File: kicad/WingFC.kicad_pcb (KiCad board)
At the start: 4 copper layers, 32 x 33.2 mm, 50 parts, among them U1 XIAO-nRF52840-Plus-SMD, U2 MP2315, U3 DPS310

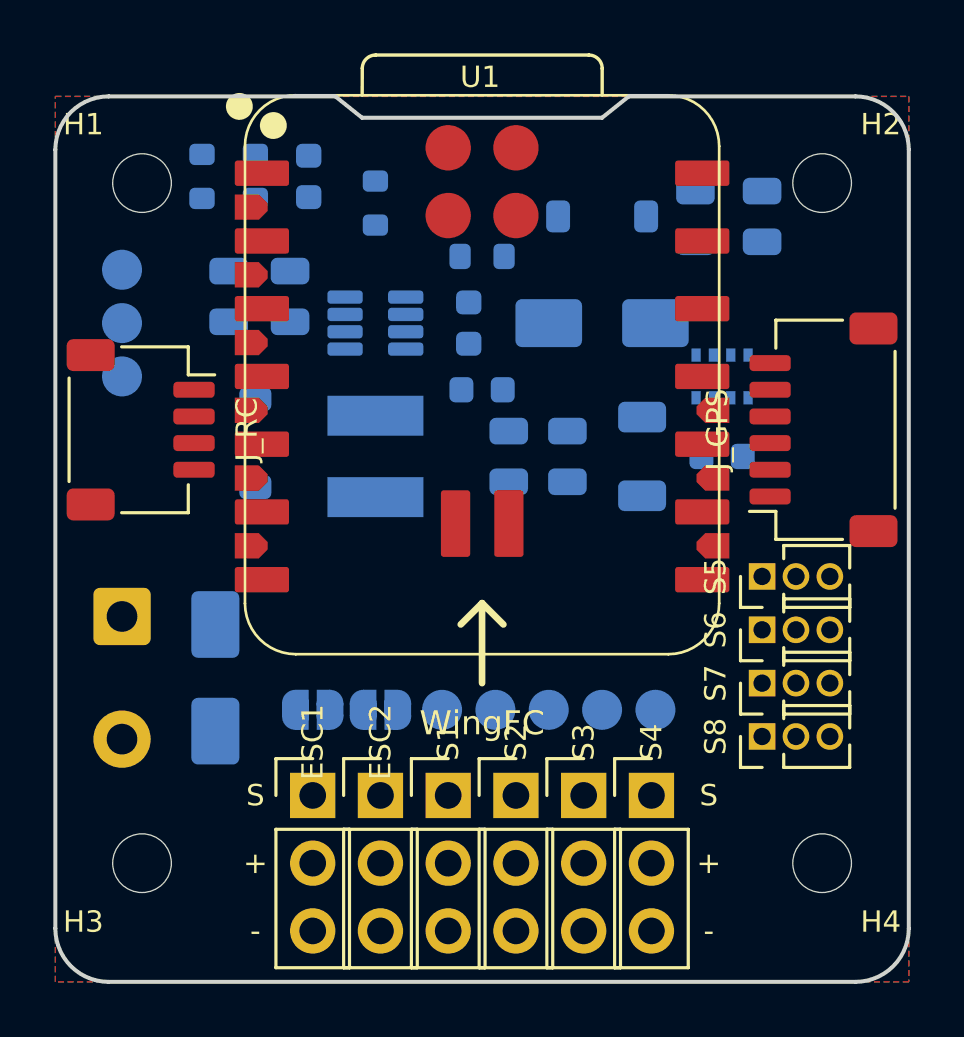
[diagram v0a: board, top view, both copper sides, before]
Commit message: fix(silkscreen): isolate flight arrow, add FerroxRC branding, and refine label clearances
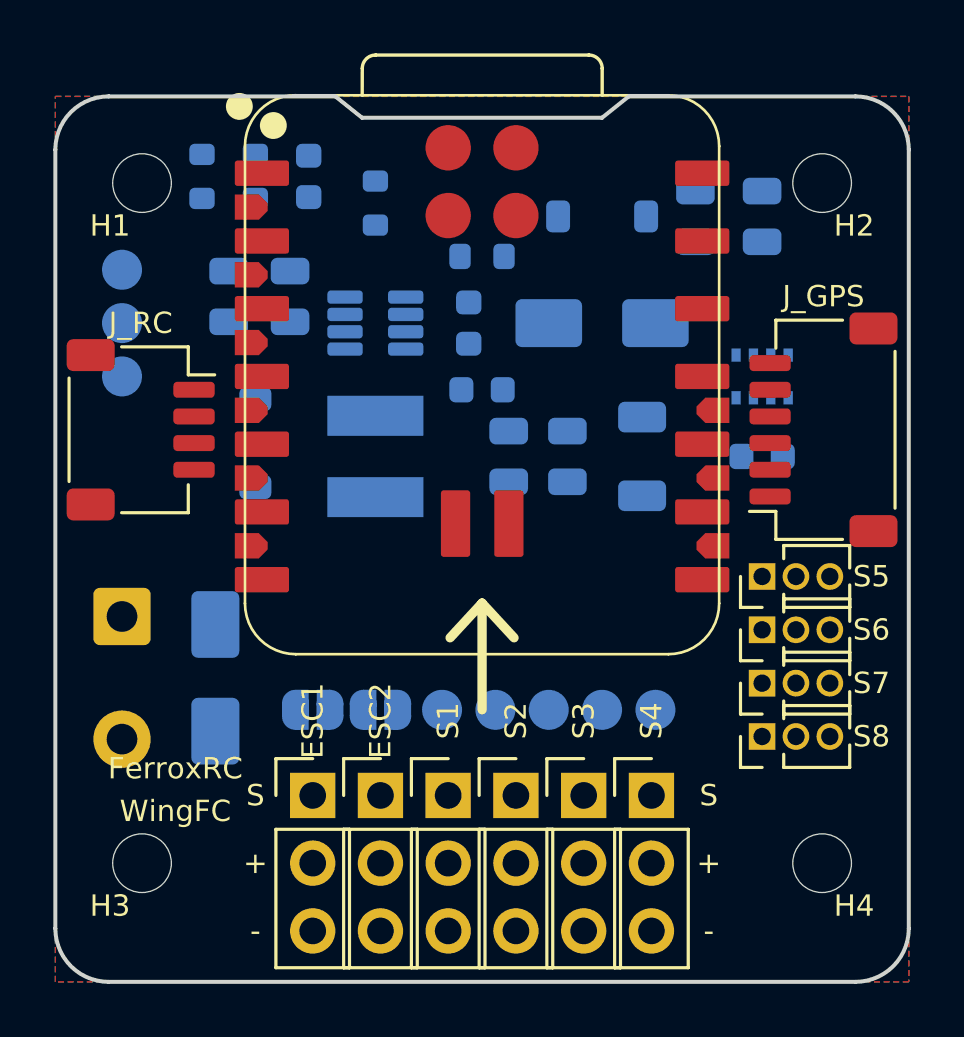
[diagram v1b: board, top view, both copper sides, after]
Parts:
- moved C7 1.50 mm to (160.5, 97.5)
- moved U3 1.50 mm to (160.5, 94.5)
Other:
- board text added: "FerroxRC"
- board text added: "FerroxRC WingFC Rev C"

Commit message: fix(silkscreen): move arrow to bottom, balance branding at H3/H4, angle actuator labels 45 deg, and add aux polarity labels
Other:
- board text added: "FerroxRC WingFC"
- board text added: "Rev C"
- board text removed: "FerroxRC WingFC Rev C"

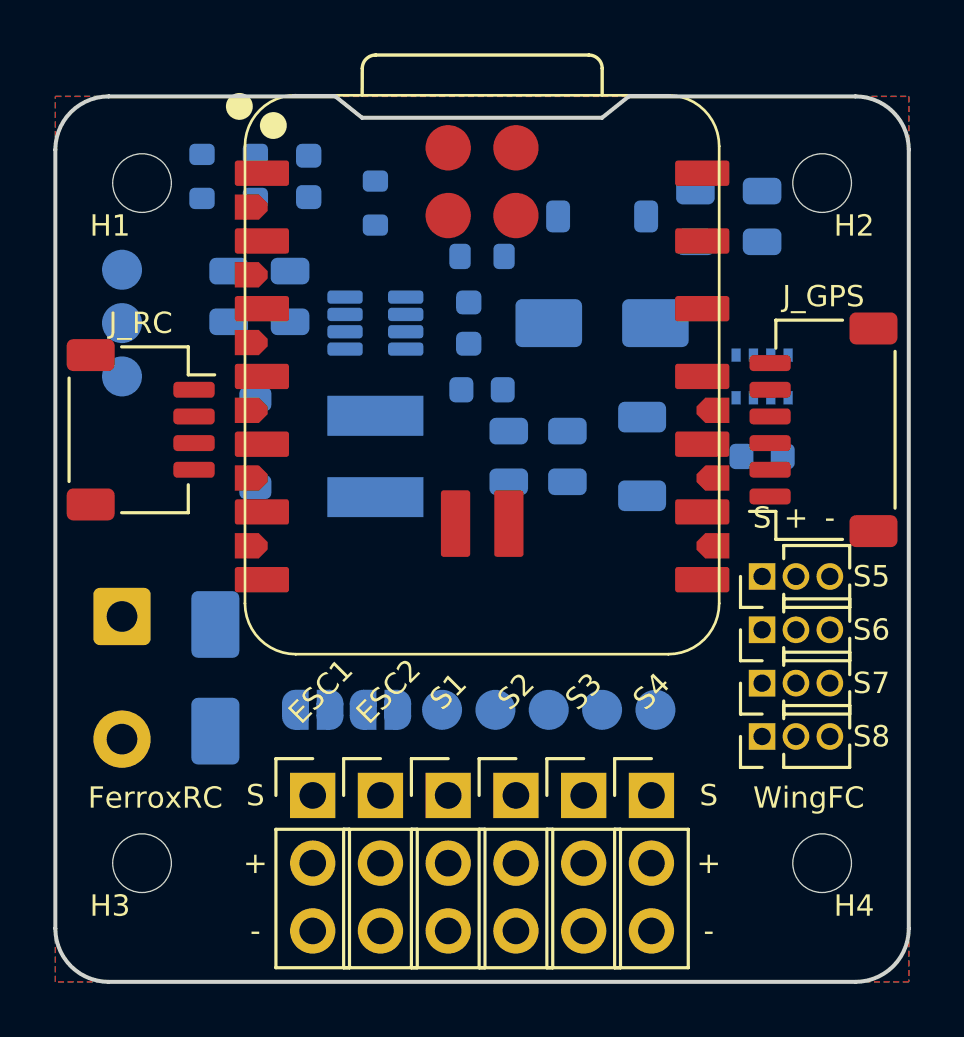
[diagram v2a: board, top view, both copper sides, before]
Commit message: WIP: first-pass routing, silkscreen cleanup, aux servo labels (DRC not yet clean)
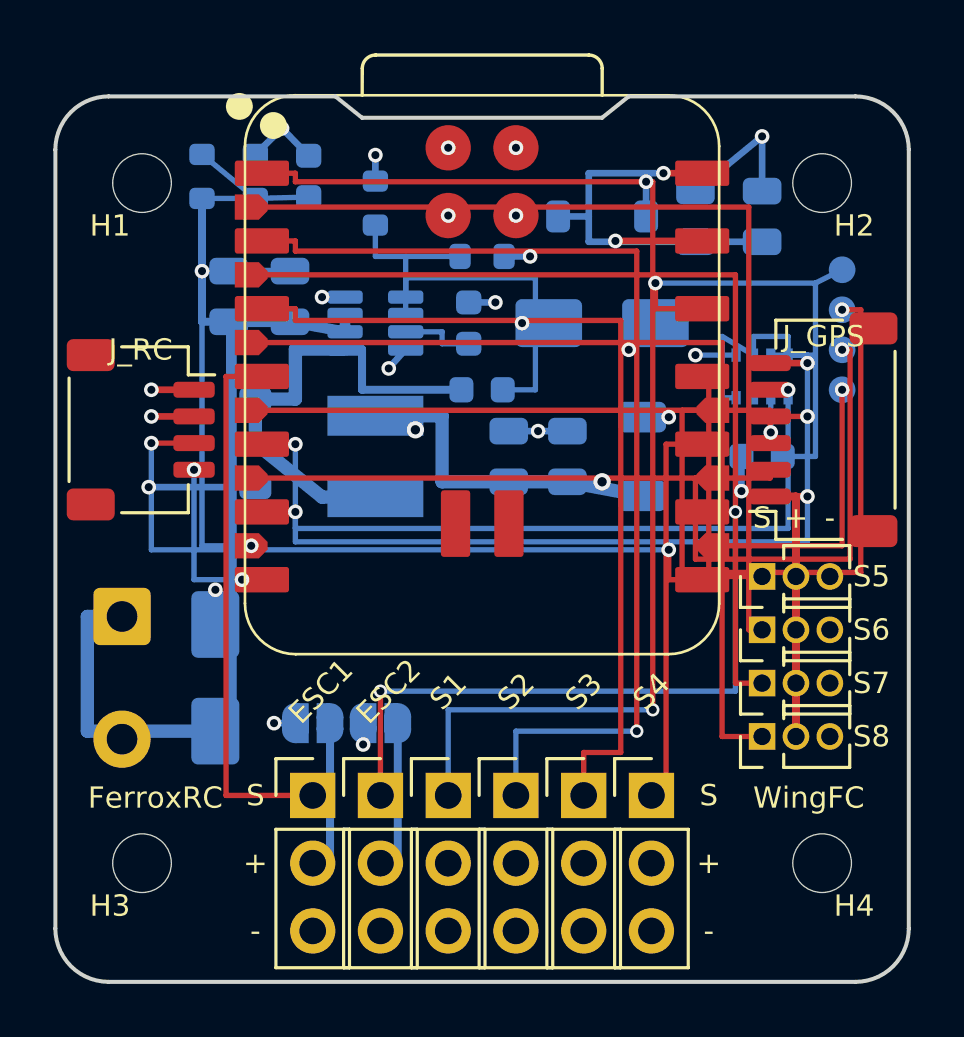
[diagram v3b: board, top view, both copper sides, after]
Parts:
- moved TP6 27.4 mm to (163.5, 95.0)
- moved TP8 27.1 mm to (163.5, 92.0)
- moved TP7 27.0 mm to (163.5, 93.5)
- moved TP2 21.1 mm to (151.3, 85.9)
- moved TP1 21.1 mm to (148.7, 85.9)
- moved TP4 19.4 mm to (148.7, 88.5)
- moved TP3 18.6 mm to (151.3, 88.5)
- moved TP5 17.9 mm to (163.5, 90.5)
- moved JP1 0.50 mm to (143.7, 107.5), turned to 0 degrees
- moved JP2 0.50 mm to (146.2, 107.5), turned to 0 degrees
- turned U2 to 0 degrees
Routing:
- net /SERVO_1: track 0.00 -> 45.7 mm, vias 0 -> 1
- net /SERVO_2: track 0.00 -> 39.4 mm, vias 0 -> 1
- net VBAT: track 0.00 -> 37.1 mm
- net GND: track 0.00 -> 35.5 mm, vias 0 -> 19
- net /SERVO_6: track 0.00 -> 35.0 mm
- net /SERVO_7: track 0.00 -> 34.5 mm
- net /SERVO_8: track 0.00 -> 33.9 mm
- net /SERVO_3: track 0.00 -> 33.1 mm
- net /I2C_SCL: track 0.00 -> 31.3 mm, vias 0 -> 2
- net +5V: track 0.00 -> 30.4 mm, vias 0 -> 9
- net /I2C_SDA: track 0.00 -> 28.5 mm, vias 0 -> 2
- net /RC_RX: track 0.00 -> 27.4 mm, vias 0 -> 2
- net +3V3: track 0.00 -> 25.5 mm, vias 0 -> 1
- net /MOTOR_2: track 0.00 -> 25.2 mm, vias 0 -> 2
- net /D19: track 0.00 -> 24.5 mm, vias 0 -> 1
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- removed copper zone on B.Cu, net GND
- removed copper zone on F.Cu, net GND
